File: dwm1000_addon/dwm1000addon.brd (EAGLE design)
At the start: 29.2 x 20.3 mm, 7 parts, among them U1 DWM1000

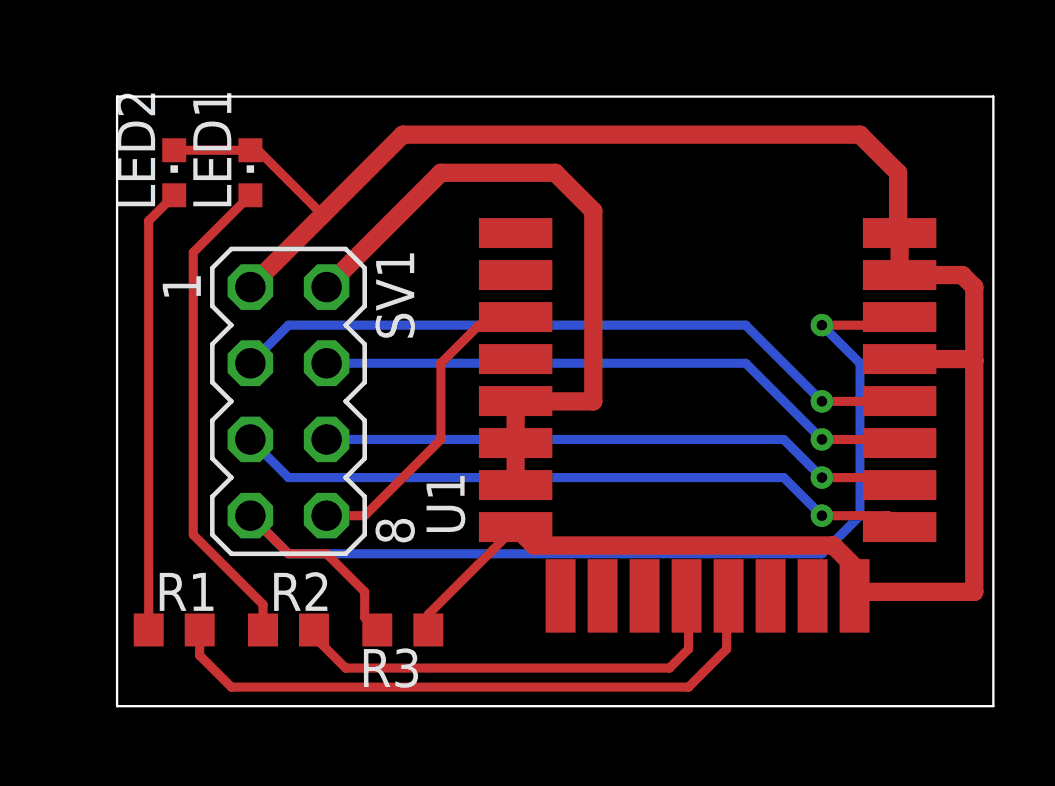
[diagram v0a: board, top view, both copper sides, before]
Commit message: dwm1000_addon: poprawione prowadzenie ścieżek masy
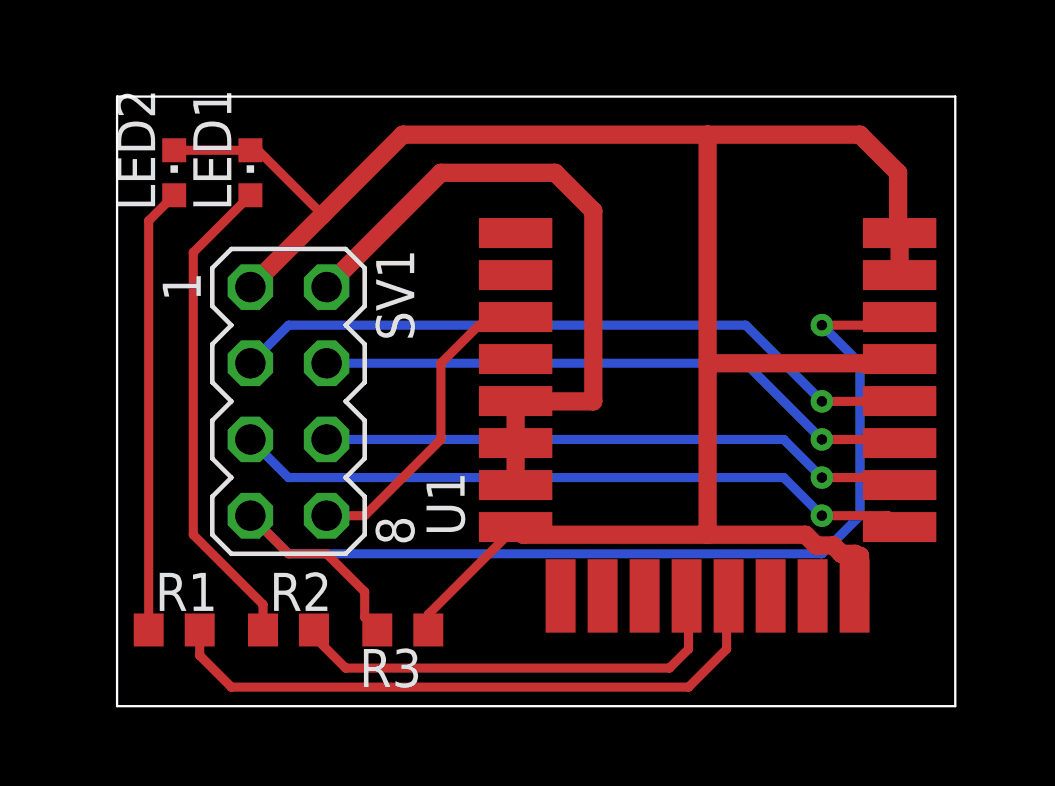
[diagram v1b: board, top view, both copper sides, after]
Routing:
- net GND: track 70.3 -> 71.2 mm
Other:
- board size 29.2 x 20.3 mm -> 27.9 x 20.3 mm
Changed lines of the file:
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@@
 <plain>
 <wire x1="10.795" y1="19.05" x2="10.795" y2="39.37" width="0.0762" layer="20"/>
-<wire x1="10.795" y1="39.37" x2="40.005" y2="39.37" width="0.0762" layer="20"/>
-<wire x1="40.005" y1="39.37" x2="40.005" y2="19.05" width="0.0762" layer="20"/>
-<wire x1="40.005" y1="19.05" x2="10.795" y2="19.05" width="0.0762" layer="20"/>
+<wire x1="10.795" y1="39.37" x2="38.735" y2="39.37" width="0.0762" layer="20"/>
+<wire x1="38.735" y1="39.37" x2="38.735" y2="19.05" width="0.0762" layer="20"/>
+<wire x1="38.735" y1="19.05" x2="10.795" y2="19.05" width="0.0762" layer="20"/>
 </plain>
 <attributes>
@@
 <contactref element="SV1" pad="1"/>
 <wire x1="36.88" y1="34.82" x2="36.88" y2="33.42" width="0.6096" layer="1"/>
-<wire x1="36.88" y1="33.42" x2="38.97" y2="33.42" width="0.6096" layer="1"/>
-<wire x1="38.97" y1="33.42" x2="39.37" y2="33.02" width="0.6096" layer="1"/>
-<wire x1="39.37" y1="30.56424375" x2="39.37" y2="33.02" width="0.6096" layer="1"/>
-<wire x1="39.37" y1="30.56424375" x2="39.37" y2="22.86" width="0.6096" layer="1"/>
-<wire x1="39.37" y1="22.86" x2="35.515" y2="22.86" width="0.6096" layer="1"/>
-<wire x1="35.515" y1="22.86" x2="35.38" y2="22.725" width="0.6096" layer="1"/>
-<wire x1="36.88" y1="30.62" x2="39.31424375" y2="30.62" width="0.6096" layer="1"/>
-<wire x1="39.31424375" y1="30.62" x2="39.37" y2="30.56424375" width="0.6096" layer="1"/>
 <wire x1="17.64728125" y1="35.42728125" x2="15.24" y2="33.02" width="0.6096" layer="1"/>
 <wire x1="17.64728125" y1="35.42728125" x2="20.32" y2="38.1" width="0.6096" layer="1"/>
-<wire x1="20.32" y1="38.1" x2="35.56" y2="38.1" width="0.6096" layer="1"/>
+<wire x1="20.32" y1="38.1" x2="30.48" y2="38.1" width="0.6096" layer="1"/>
+<wire x1="30.48" y1="38.1" x2="35.56" y2="38.1" width="0.6096" layer="1"/>
 <wire x1="35.56" y1="38.1" x2="36.83" y2="36.83" width="0.6096" layer="1"/>
 <wire x1="36.83" y1="36.83" x2="36.83" y2="34.87" width="0.6096" layer="1"/>
@@
 <wire x1="21.17" y1="21.59" x2="21.17" y2="22.11" width="0.3048" layer="1"/>
 <wire x1="24.08" y1="25.02" x2="21.17" y2="22.11" width="0.3048" layer="1"/>
-<wire x1="35.38" y1="22.725" x2="35.38" y2="23.69658125" width="0.6096" layer="1"/>
-<wire x1="35.38" y1="23.69658125" x2="34.66938125" y2="24.4072" width="0.6096" layer="1"/>
-<wire x1="24.6928" y1="24.4072" x2="24.08" y2="25.02" width="0.6096" layer="1"/>
-<wire x1="34.66938125" y1="24.4072" x2="24.6928" y2="24.4072" width="0.6096" layer="1"/>
 <wire x1="12.7" y1="37.58" x2="15.24" y2="37.58" width="0.3048" layer="1"/>
 <wire x1="15.24" y1="37.58" x2="15.4945625" y2="37.58" width="0.3048" layer="1"/>
 <wire x1="15.4945625" y1="37.58" x2="17.64728125" y2="35.42728125" width="0.3048" layer="1"/>
+<wire x1="30.48" y1="38.1" x2="30.48" y2="30.48" width="0.6096" layer="1"/>
+<wire x1="30.48" y1="30.48" x2="36.74" y2="30.48" width="0.6096" layer="1"/>
+<wire x1="36.74" y1="30.48" x2="36.88" y2="30.62" width="0.6096" layer="1"/>
+<wire x1="24.335" y1="24.765" x2="30.48" y2="24.765" width="0.6096" layer="1"/>
+<wire x1="24.335" y1="24.765" x2="24.08" y2="25.02" width="0.6096" layer="1"/>
+<wire x1="30.48" y1="30.48" x2="30.48" y2="24.765" width="0.6096" layer="1"/>
+<wire x1="30.48" y1="24.765" x2="33.7435625" y2="24.765" width="0.6096" layer="1"/>
+<wire x1="34.66938125" y1="24.4072" x2="34.9372" y2="24.13938125" width="0.6096" layer="1"/>
+<wire x1="34.9372" y1="24.13938125" x2="34.9372" y2="24.13" width="0.6096" layer="1"/>
+<wire x1="33.7435625" y1="24.765" x2="34.1013625" y2="24.4072" width="0.6096" layer="1"/>
+<wire x1="34.1013625" y1="24.4072" x2="34.66938125" y2="24.4072" width="0.6096" layer="1"/>
+<wire x1="34.9372" y1="24.13" x2="35.39841875" y2="24.13" width="0.6096" layer="1"/>
+<wire x1="35.39841875" y1="24.13" x2="35.46561875" y2="24.0628" width="0.6096" layer="1"/>
+<wire x1="35.46561875" y1="24.0628" x2="35.56" y2="24.0628" width="0.6096" layer="1"/>
+<wire x1="35.56" y1="24.0628" x2="35.56" y2="22.905" width="0.6096" layer="1"/>
+<wire x1="35.56" y1="22.905" x2="35.38" y2="22.725" width="0.6096" layer="1"/>
 </signal>
 <signal name="N$6">

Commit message: dwm1000_addon: zmniejszone pole masy pod anteną, przesunięte diody aktywności
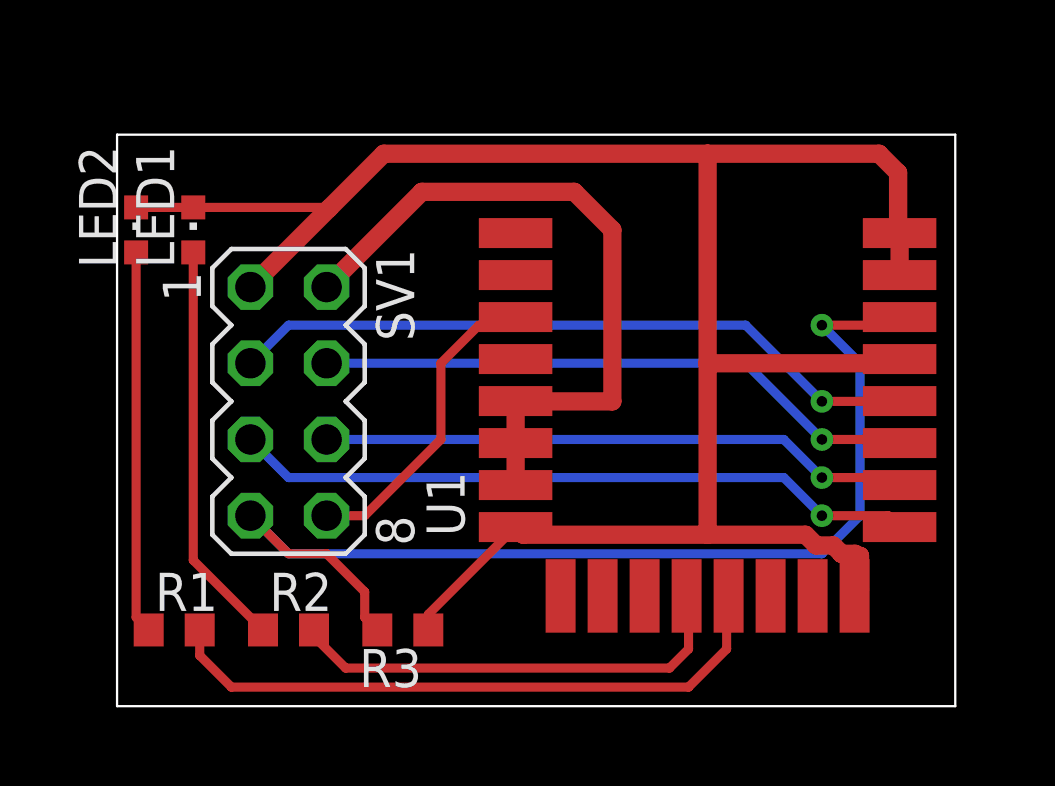
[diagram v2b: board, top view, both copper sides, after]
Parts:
- moved LED1 2.69 mm to (13.3, 34.9)
- moved LED2 2.29 mm to (11.4, 34.9)
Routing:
- net N$12: track 16.2 -> 13.5 mm
- net N$6: track 14.8 -> 12.8 mm
- net GND: track 71.2 -> 70.7 mm
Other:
- board size 27.9 x 20.3 mm -> 27.9 x 19.1 mm
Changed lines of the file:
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@@
 <board>
 <plain>
-<wire x1="10.795" y1="19.05" x2="10.795" y2="39.37" width="0.0762" layer="20"/>
-<wire x1="10.795" y1="39.37" x2="38.735" y2="39.37" width="0.0762" layer="20"/>
-<wire x1="38.735" y1="39.37" x2="38.735" y2="19.05" width="0.0762" layer="20"/>
+<wire x1="10.795" y1="19.05" x2="10.795" y2="38.1" width="0.0762" layer="20"/>
+<wire x1="10.795" y1="38.1" x2="38.735" y2="38.1" width="0.0762" layer="20"/>
+<wire x1="38.735" y1="38.1" x2="38.735" y2="19.05" width="0.0762" layer="20"/>
 <wire x1="38.735" y1="19.05" x2="10.795" y2="19.05" width="0.0762" layer="20"/>
 </plain>
@@
 </autorouter>
 <elements>
-<element name="LED1" library="led" library_urn="urn:adsk.eagle:library:259" package="CHIPLED_0603" value="" x="15.24" y="36.83"/>
-<element name="LED2" library="led" library_urn="urn:adsk.eagle:library:259" package="CHIPLED_0603" value="" x="12.7" y="36.83"/>
+<element name="LED1" library="led" library_urn="urn:adsk.eagle:library:259" package="CHIPLED_0603" value="" x="13.335" y="34.925"/>
+<element name="LED2" library="led" library_urn="urn:adsk.eagle:library:259" package="CHIPLED_0603" value="" x="11.43" y="34.925"/>
 <element name="R1" library="resistor" library_urn="urn:adsk.eagle:library:348" package="R0603" value="330R" x="12.7" y="21.59"/>
 <element name="R2" library="resistor" library_urn="urn:adsk.eagle:library:348" package="R0603" value="330R" x="16.51" y="21.59"/>
@@
 <wire x1="24.08" y1="29.22" x2="24.08" y2="27.82" width="0.6096" layer="1"/>
 <wire x1="24.08" y1="27.82" x2="24.08" y2="26.42" width="0.6096" layer="1"/>
-<wire x1="17.78" y1="33.02" x2="21.59" y2="36.83" width="0.6096" layer="1"/>
-<wire x1="21.59" y1="36.83" x2="25.4" y2="36.83" width="0.6096" layer="1"/>
-<wire x1="25.4" y1="36.83" x2="26.67" y2="35.56" width="0.6096" layer="1"/>
-<wire x1="26.67" y1="29.21" x2="24.09" y2="29.21" width="0.6096" layer="1"/>
+<wire x1="17.78" y1="33.02" x2="20.955" y2="36.195" width="0.6096" layer="1"/>
+<wire x1="20.955" y1="36.195" x2="26.035" y2="36.195" width="0.6096" layer="1"/>
+<wire x1="26.035" y1="36.195" x2="27.305" y2="34.925" width="0.6096" layer="1"/>
+<wire x1="27.305" y1="29.21" x2="24.09" y2="29.21" width="0.6096" layer="1"/>
 <wire x1="24.09" y1="29.21" x2="24.08" y2="29.22" width="0.6096" layer="1"/>
-<wire x1="26.67" y1="35.56" x2="26.67" y2="29.21" width="0.6096" layer="1"/>
+<wire x1="27.305" y1="34.925" x2="27.305" y2="29.21" width="0.6096" layer="1"/>
 </signal>
 <signal name="GND">
@@
 <contactref element="SV1" pad="1"/>
 <wire x1="36.88" y1="34.82" x2="36.88" y2="33.42" width="0.6096" layer="1"/>
-<wire x1="17.64728125" y1="35.42728125" x2="15.24" y2="33.02" width="0.6096" layer="1"/>
-<wire x1="17.64728125" y1="35.42728125" x2="20.32" y2="38.1" width="0.6096" layer="1"/>
-<wire x1="20.32" y1="38.1" x2="30.48" y2="38.1" width="0.6096" layer="1"/>
-<wire x1="30.48" y1="38.1" x2="35.56" y2="38.1" width="0.6096" layer="1"/>
-<wire x1="35.56" y1="38.1" x2="36.83" y2="36.83" width="0.6096" layer="1"/>
+<wire x1="17.861884375" y1="35.641884375" x2="15.24" y2="33.02" width="0.6096" layer="1"/>
+<wire x1="17.861884375" y1="35.641884375" x2="19.685" y2="37.465" width="0.6096" layer="1"/>
+<wire x1="19.685" y1="37.465" x2="30.48" y2="37.465" width="0.6096" layer="1"/>
+<wire x1="30.48" y1="37.465" x2="36.195" y2="37.465" width="0.6096" layer="1"/>
+<wire x1="36.195" y1="37.465" x2="36.83" y2="36.83" width="0.6096" layer="1"/>
 <wire x1="36.83" y1="36.83" x2="36.83" y2="34.87" width="0.6096" layer="1"/>
 <wire x1="36.83" y1="34.87" x2="36.88" y2="34.82" width="0.6096" layer="1"/>
 <wire x1="21.17" y1="21.59" x2="21.17" y2="22.11" width="0.3048" layer="1"/>
 <wire x1="24.08" y1="25.02" x2="21.17" y2="22.11" width="0.3048" layer="1"/>
-<wire x1="12.7" y1="37.58" x2="15.24" y2="37.58" width="0.3048" layer="1"/>
-<wire x1="15.24" y1="37.58" x2="15.4945625" y2="37.58" width="0.3048" layer="1"/>
-<wire x1="15.4945625" y1="37.58" x2="17.64728125" y2="35.42728125" width="0.3048" layer="1"/>
-<wire x1="30.48" y1="38.1" x2="30.48" y2="30.48" width="0.6096" layer="1"/>
+<wire x1="30.48" y1="37.465" x2="30.48" y2="30.48" width="0.6096" layer="1"/>
 <wire x1="30.48" y1="30.48" x2="36.74" y2="30.48" width="0.6096" layer="1"/>
 <wire x1="36.74" y1="30.48" x2="36.88" y2="30.62" width="0.6096" layer="1"/>
@@
 <wire x1="35.56" y1="24.0628" x2="35.56" y2="22.905" width="0.6096" layer="1"/>
 <wire x1="35.56" y1="22.905" x2="35.38" y2="22.725" width="0.6096" layer="1"/>
+<wire x1="13.324721875" y1="35.675" x2="13.335" y2="35.675" width="0.1524" layer="1"/>
+<wire x1="11.43" y1="35.675" x2="13.324721875" y2="35.675" width="0.3048" layer="1"/>
+<wire x1="13.335" y1="35.675" x2="17.82876875" y2="35.675" width="0.3048" layer="1"/>
+<wire x1="17.82876875" y1="35.675" x2="17.861884375" y2="35.641884375" width="0.3048" layer="1"/>
 </signal>
 <signal name="N$6">
 <contactref element="R1" pad="1"/>
 <contactref element="LED2" pad="A"/>
-<wire x1="11.85" y1="21.59" x2="11.85" y2="35.23" width="0.3048" layer="1"/>
-<wire x1="11.85" y1="35.23" x2="12.7" y2="36.08" width="0.3048" layer="1"/>
+<wire x1="11.43" y1="34.175" x2="11.43" y2="22.01" width="0.3048" layer="1"/>
+<wire x1="11.43" y1="22.01" x2="11.85" y2="21.59" width="0.3048" layer="1"/>
 </signal>
 <signal name="N$12">
 <contactref element="R2" pad="1"/>
 <contactref element="LED1" pad="A"/>
-<wire x1="15.66" y1="21.59" x2="15.66" y2="22.44" width="0.3048" layer="1"/>
-<wire x1="15.66" y1="22.44" x2="13.335" y2="24.765" width="0.3048" layer="1"/>
-<wire x1="13.335" y1="24.765" x2="13.335" y2="34.175" width="0.3048" layer="1"/>
-<wire x1="13.335" y1="34.175" x2="15.24" y2="36.08" width="0.3048" layer="1"/>
+<wire x1="13.335" y1="34.175" x2="13.335" y2="23.915" width="0.3048" layer="1"/>
+<wire x1="13.335" y1="23.915" x2="15.66" y2="21.59" width="0.3048" layer="1"/>
 </signal>
 </signals>

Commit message: dwm1000 addon: dodane pola masy
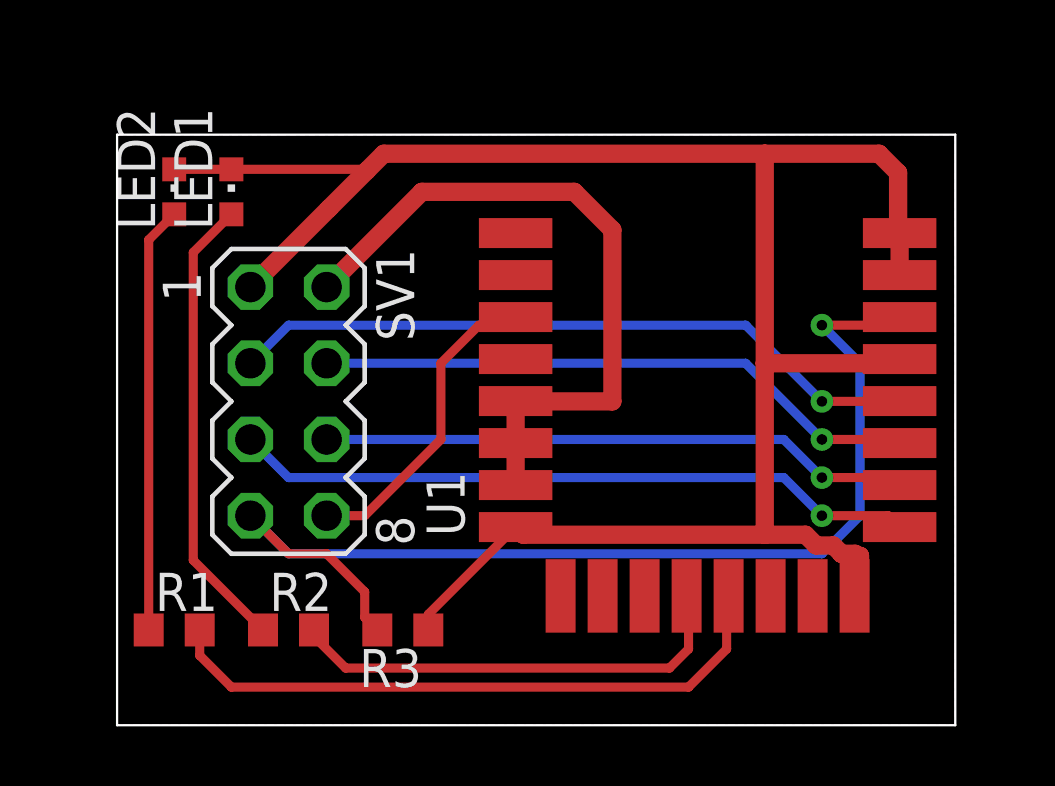
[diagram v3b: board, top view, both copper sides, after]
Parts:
- moved LED1 1.80 mm to (14.6, 36.2)
- moved LED2 1.80 mm to (12.7, 36.2)
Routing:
- net GND: track 70.7 -> 68.8 mm
- net N$12: track 13.5 -> 15.3 mm
- net N$6: track 12.8 -> 14.2 mm
- added copper zone on layer 1, net GND
- added copper zone on layer 16, net GND
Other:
- board size 27.9 x 19.1 mm -> 27.9 x 19.7 mm
